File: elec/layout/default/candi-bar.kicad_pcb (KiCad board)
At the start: 4 copper layers, 88 x 44 mm, 65 parts, among them J1 ?, J2 ?, J3 ?, J4 ?, J5 ?, J6 ?, J7 ?, U1 ?, U10 ?, U11 ?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

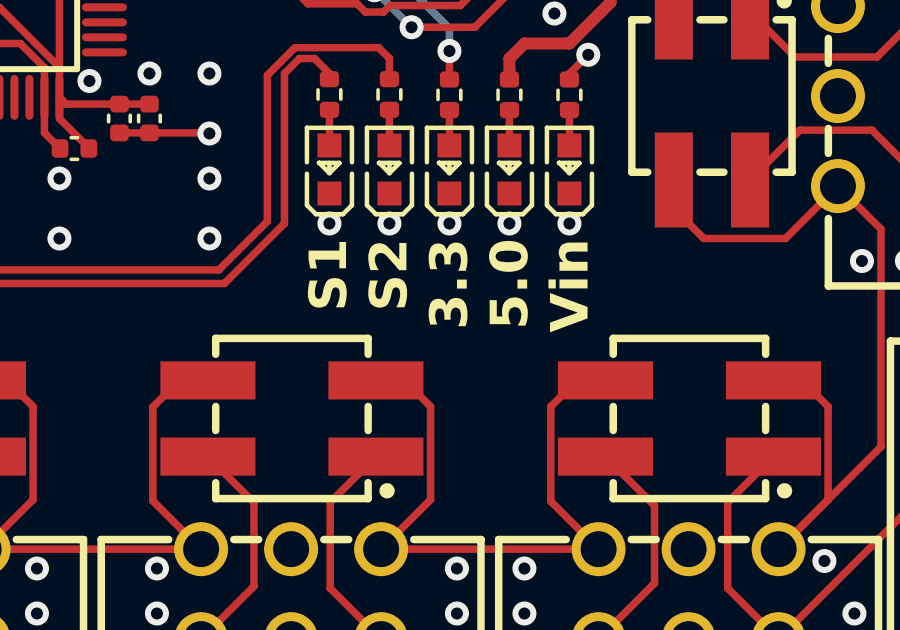
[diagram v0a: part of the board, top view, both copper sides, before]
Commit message: chore: Switch to ato v3
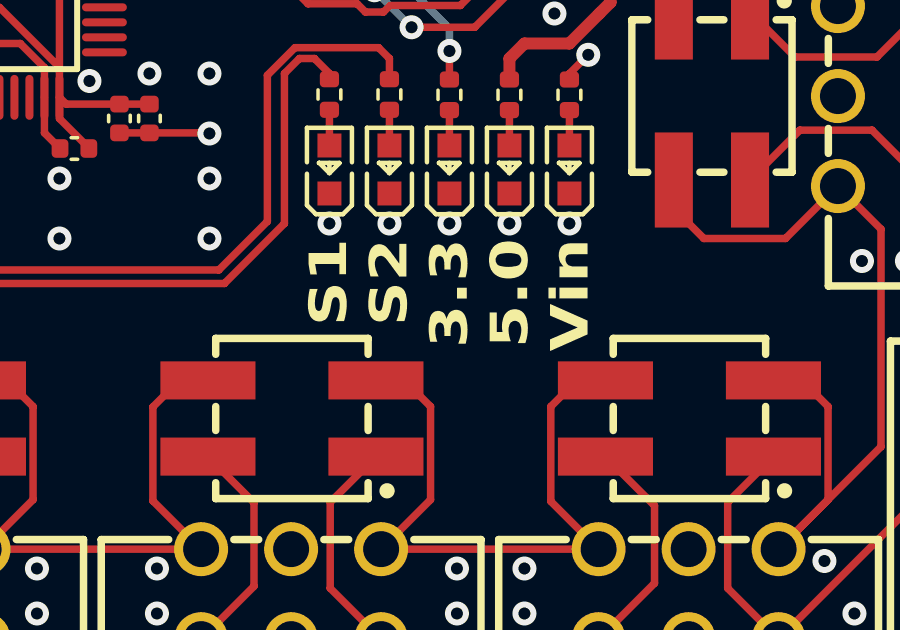
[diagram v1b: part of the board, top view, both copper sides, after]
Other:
- board text added: "CANdiBar, rev 9d5d3f4 https://github.com/CRTified/CANdiBar MIT License"
- board text removed: "CANdiBar, rev {{GITHASH}} https://github.com/CRTified/CANdiBar MIT License"

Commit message: fix: Re-add template for GITHASH
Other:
- board text added: "CANdiBar, rev {{GITHASH}} https://github.com/CRTified/CANdiBar MIT License"
- board text removed: "CANdiBar, rev 9d5d3f4 https://github.com/CRTified/CANdiBar MIT License"

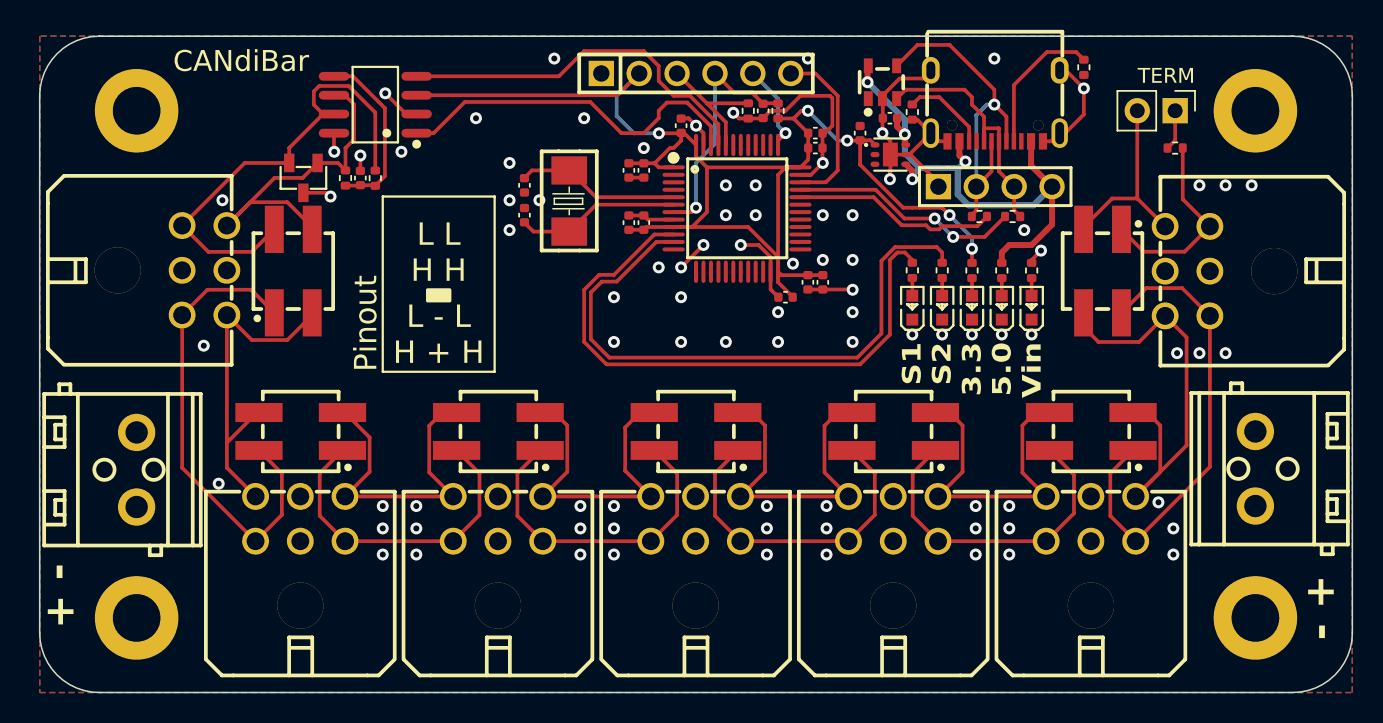
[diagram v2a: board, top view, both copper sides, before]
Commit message: feat: Allow larger tolerance of status led current
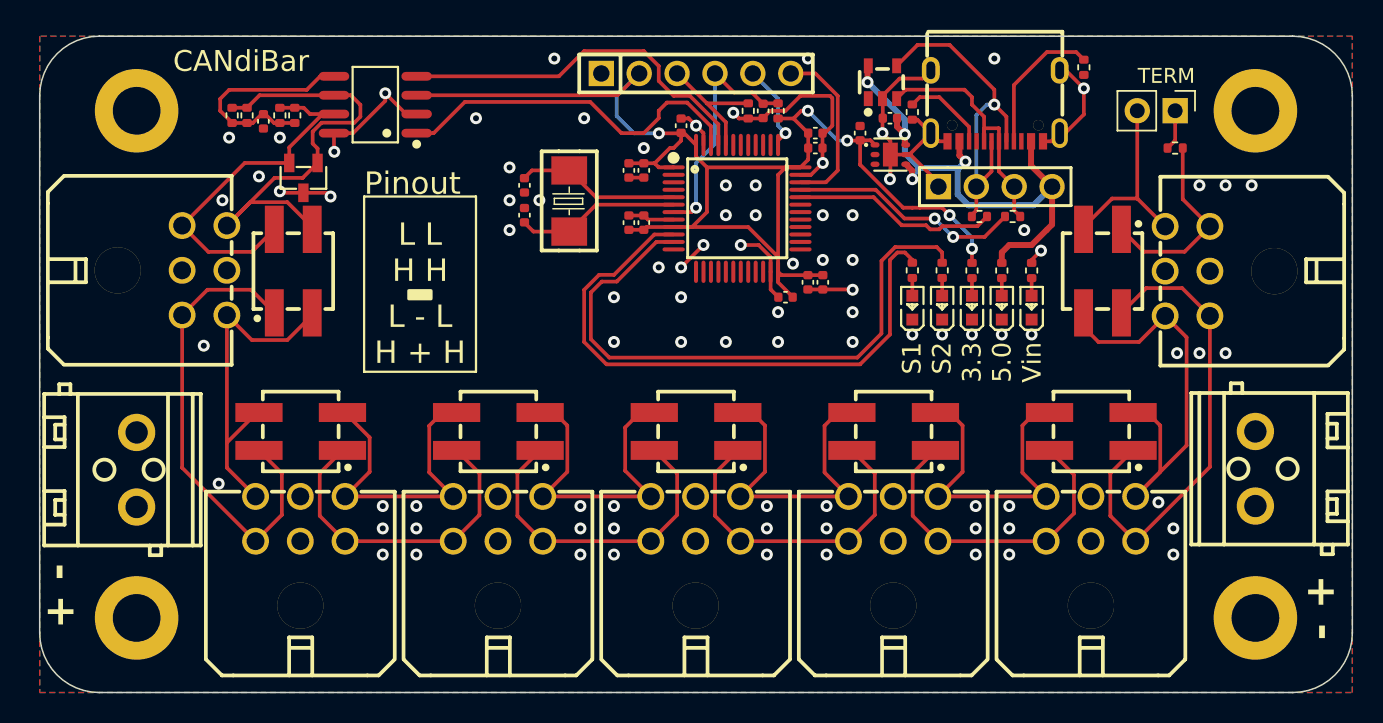
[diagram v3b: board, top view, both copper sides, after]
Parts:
- added R10: 62.5mW Thick Film Resistors 50V ±100ppm/℃ ±1% 120Ω 0402 Chi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, lib:R0402, F.Cu at (106.4, 61.3)
- added R8: 62.5mW Thick Film Resistors 50V ±100ppm/℃ ±1% 120Ω 0402 Chi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, lib:R0402, F.Cu at (109.6, 61.3)
- R13: renamed from R11; value 62.5mW Thick Film Resistors 50V ±100ppm/℃ ±1% 470Ω 0402 Chip Resistor - Surface Mount ROHS -> 62.5mW Thick Film Resistors 50V ±100ppm/℃ ±1% 510Ω 0402 Chip Resistor - Surface Mount ROHS
- R14: renamed from R12; value 62.5mW Thick Film Resistors 50V ±100ppm/℃ ±1% 470Ω 0402 Chip Resistor - Surface Mount ROHS -> 62.5mW Thick Film Resistors 50V ±100ppm/℃ ±1% 510Ω 0402 Chip Resistor - Surface Mount ROHS
- R4: value 62.5mW Thick Film Resistors 50V ±100ppm/℃ ±1% 6.8kΩ 0402 Chip Resistor - Surface Mount ROHS -> 62.5mW Thick Film Resistors 50V ±100ppm/℃ ±1% 10kΩ 0402 Chip Resistor - Surface Mount ROHS
- R5: value 62.5mW Thick Film Resistors 50V ±100ppm/℃ ±1% 470Ω 0402 Chip Resistor - Surface Mount ROHS -> 62.5mW Thick Film Resistors 50V ±100ppm/℃ ±1% 510Ω 0402 Chip Resistor - Surface Mount ROHS
- R7: value 62.5mW Thick Film Resistors 50V ±100ppm/℃ ±1% 60.4Ω 0402 Chip Resistor - Surface Mount ROHS -> 62.5mW Thick Film Resistors 50V ±100ppm/℃ ±1% 120Ω 0402 Chip Resistor - Surface Mount ROHS
- R9: renamed from R8; value 62.5mW Thick Film Resistors 50V ±100ppm/℃ ±1% 60.4Ω 0402 Chip Resistor - Surface Mount ROHS -> 62.5mW Thick Film Resistors 50V ±100ppm/℃ ±1% 120Ω 0402 Chip Resistor - Surface Mount ROHS
- moved R9 7.82 mm to (107.4, 61.3)
- moved C12 7.53 mm to (108.5, 61.7), turned to -90 degrees
- moved R7 6.85 mm to (110.6, 61.3)
- renumbered R9 to R11, R10 to R12, R13 to R15, R14 to R16
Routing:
- net canl: track 23.4 -> 30.9 mm
- net canh: track 32.1 -> 26.0 mm
- net gnd: track 65.7 -> 71.2 mm, vias 86 -> 88
- net candi_u2c.can_trx.ic-vcc: track 11.8 -> 14.9 mm

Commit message: feat: Switch to other screw terminal for power
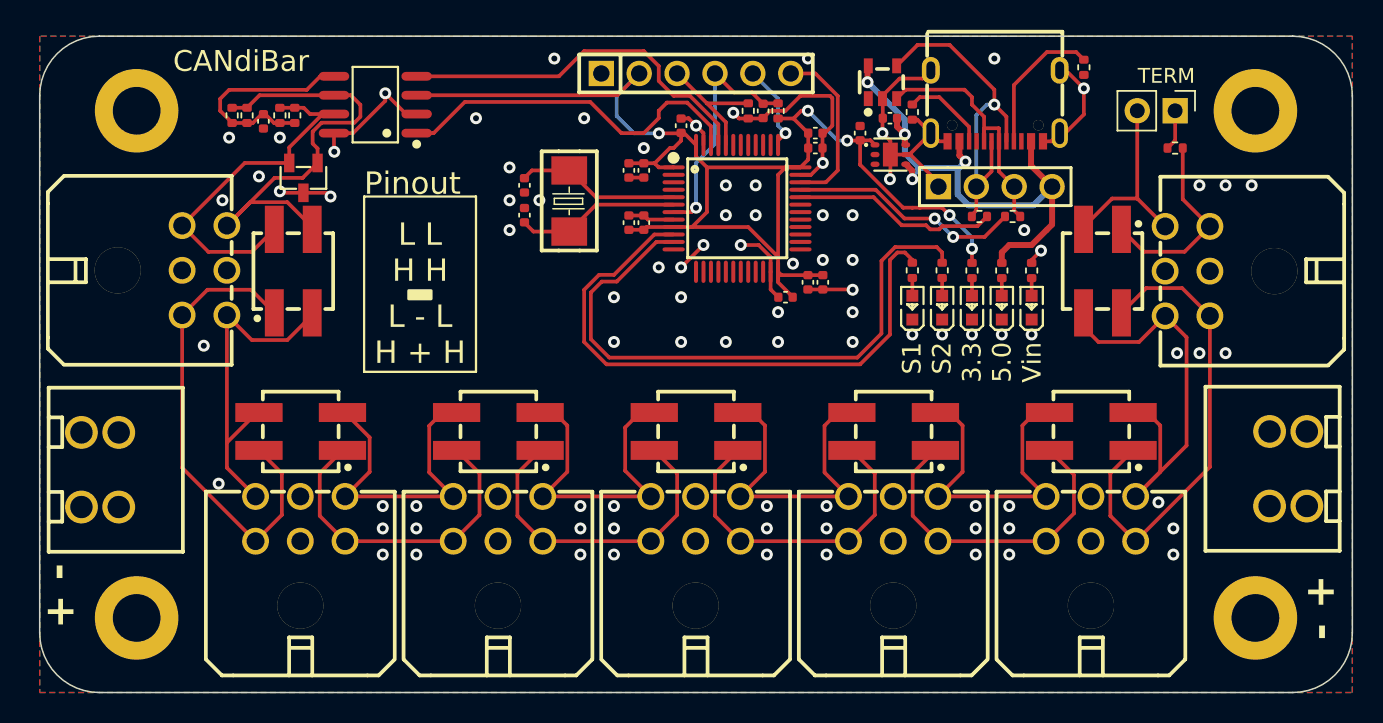
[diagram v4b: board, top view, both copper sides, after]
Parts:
- U5, U6: footprint lib:CONN-TH_2P-P5.00_DB129V-5.0-2P-BK-S -> lib:CONN-TH_978-Y-02
- moved U5 2.45 mm to (97.5, 85.1)
- moved U6 2.20 mm to (177.2, 85.0)

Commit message: fix: Switch to bigger termination resistors to be able to handle a fault
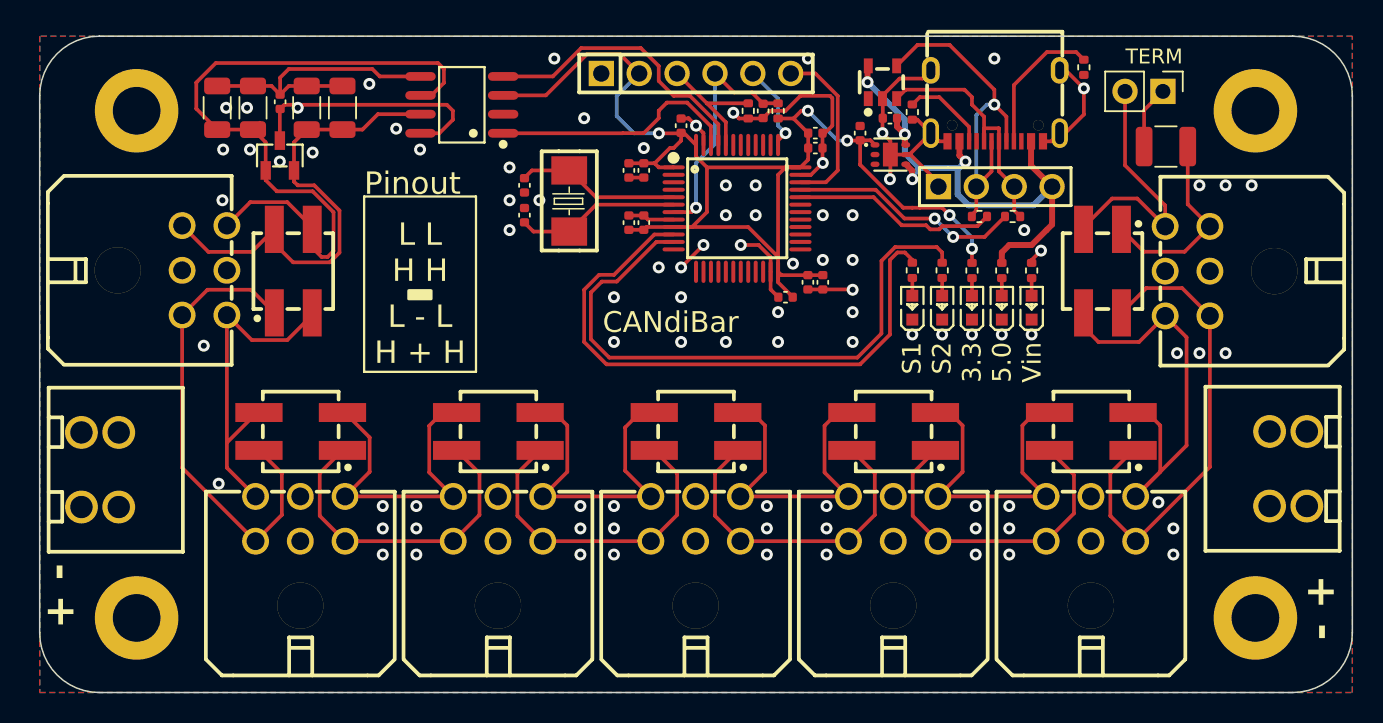
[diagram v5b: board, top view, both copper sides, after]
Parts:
- R10, R7, R8, R9: value 62.5mW Thick Film Resistors 50V ±100ppm/℃ ±1% 120Ω 0402 Chip Resistor - Surface Mount ROHS -> 250mW Thick Film Resistors 200V ±100ppm/℃ ±1% 120Ω 1206 Chip Resistor - Surface Mount ROHS; footprint lib:R0402 -> lib:R1206
- R16: value 62.5mW Thick Film Resistors 50V ±100ppm/℃ ±1% 120Ω 0402 Chip Resistor - Surface Mount ROHS -> 333.333mW Thick Film Resistors 200V ±100ppm/℃ ±1% 120Ω 1210 Chip Resistor - Surface Mount ROHS; footprint lib:R0402 -> lib:R1210
- moved U16 5.80 mm to (121.8, 60.6)
- moved R8 4.23 mm to (113.8, 60.8), turned to 90 degrees
- moved U17 2.18 mm to (109.6, 64.0), turned to -90 degrees
- moved R9 2.06 mm to (105.4, 60.8), turned to 90 degrees
- moved C12 1.72 mm to (109.6, 60.4)
- moved JP8 1.54 mm to (168.8, 59.7)
- moved R10 1.49 mm to (107.8, 60.8), turned to 90 degrees
- moved R7 0.95 mm to (111.4, 60.8), turned to 90 degrees
- moved R16 0.63 mm to (169.0, 63.4)
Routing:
- net canl: track 30.9 -> 49.0 mm
- net pb9: track 24.5 -> 17.0 mm
- net canh: track 26.0 -> 32.2 mm
- net pb8: track 24.9 -> 19.3 mm
- net candi_u2c.can_trx.ic-vcc: track 14.9 -> 19.9 mm
- net gnd: track 71.2 -> 76.0 mm, vias 88 -> 90
- net vcc-1: track 92.5 -> 87.7 mm
- net canl-7: track 13.1 -> 17.4 mm
- net p1: track 2.71 -> 4.22 mm

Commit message: docs: Update pictures
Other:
- board text added: "CANdiBar rev {{GITHASH}} https://github.com/CRTified/CANdiBar MIT License"
- board text removed: "CANdiBar, rev {{GITHASH}} https://github.com/CRTified/CANdiBar MIT License"

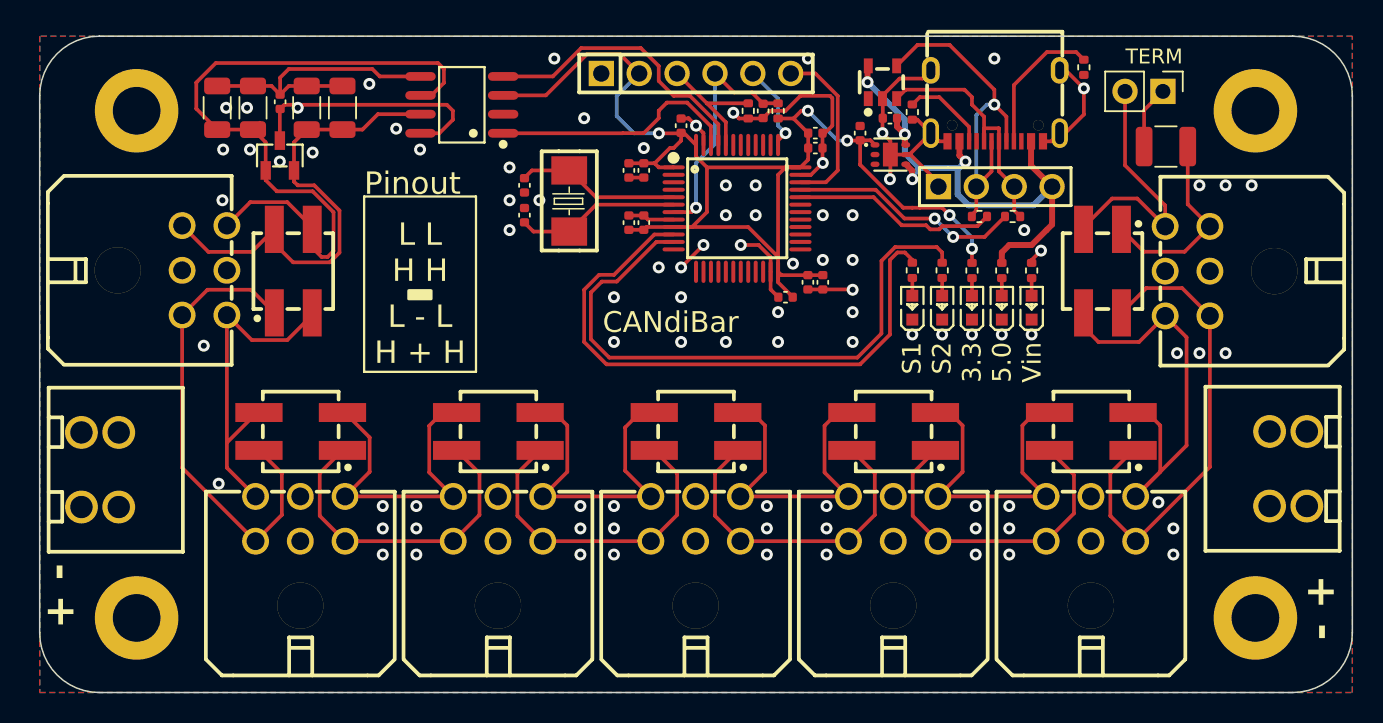
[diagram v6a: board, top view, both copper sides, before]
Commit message: fix: Change silkscreen on left power input
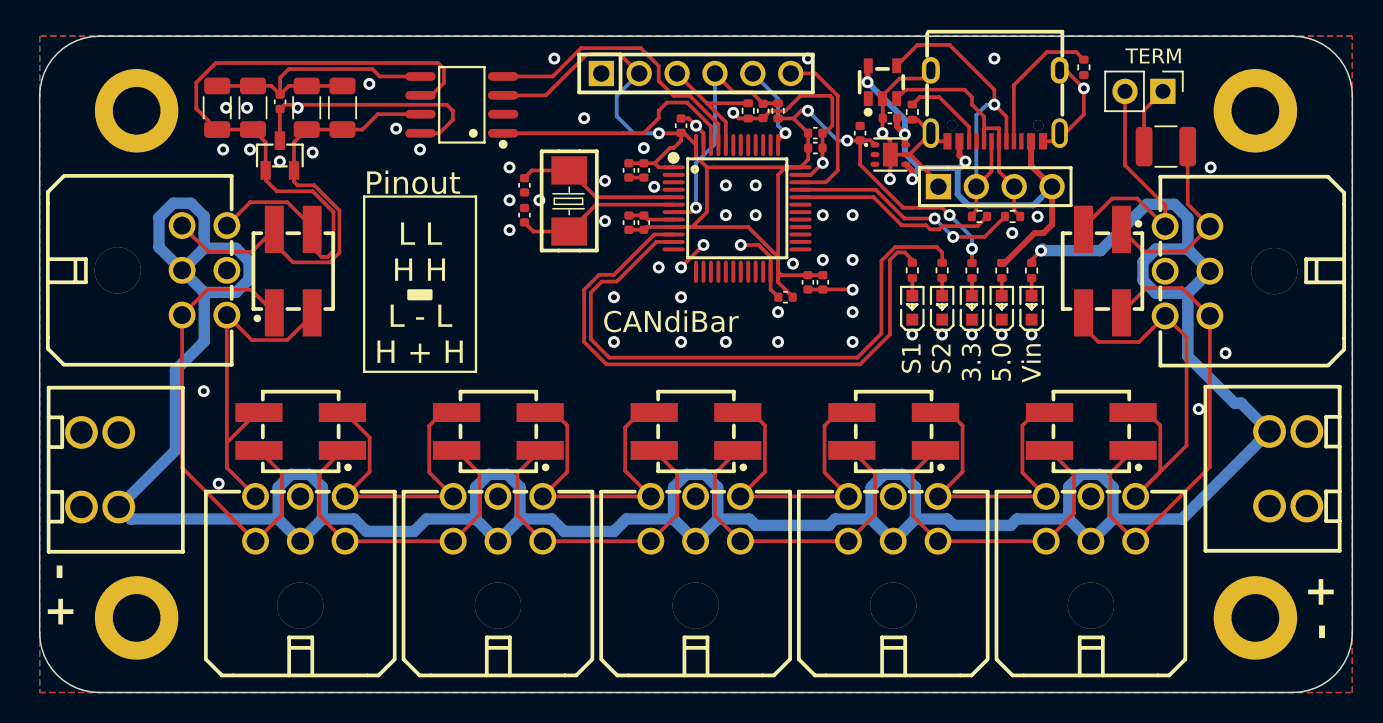
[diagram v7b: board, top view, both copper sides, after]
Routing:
- net vcc: track 1.08 -> 205.6 mm
- net gnd: vias 90 -> 63
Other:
- board text added: "+ -"
